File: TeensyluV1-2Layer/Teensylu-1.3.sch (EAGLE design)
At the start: 101 parts, among them J1 M02POLAR, J11 M02POLAR, J12 M02POLAR, J2 MICROSD, J3 USB-MICRO-PTH, J4 M02POLAR, J5 4P-TERM-BLOCK284391-4, J6 39-29-3066, J7 HOTEND-1, J8 2x7, J9 HOTBED, P1 POLOLU-X, P2 POLOLU-Y, P3 POLOLU-Z, P4 POLOLU-E1, Q1 PMV45EN, Q2 PSMN1R2-30YLC, Q3 PSMN1R2-30YLC, Q5 MMUN2211LT3G, U1 LMR16006X, U2 PRTR5V0U4DSOT23-6, U3 AP7313SOT23C, U4 TXB0104TSSOP14, U5 AT90USB1286, X1 16MHZ

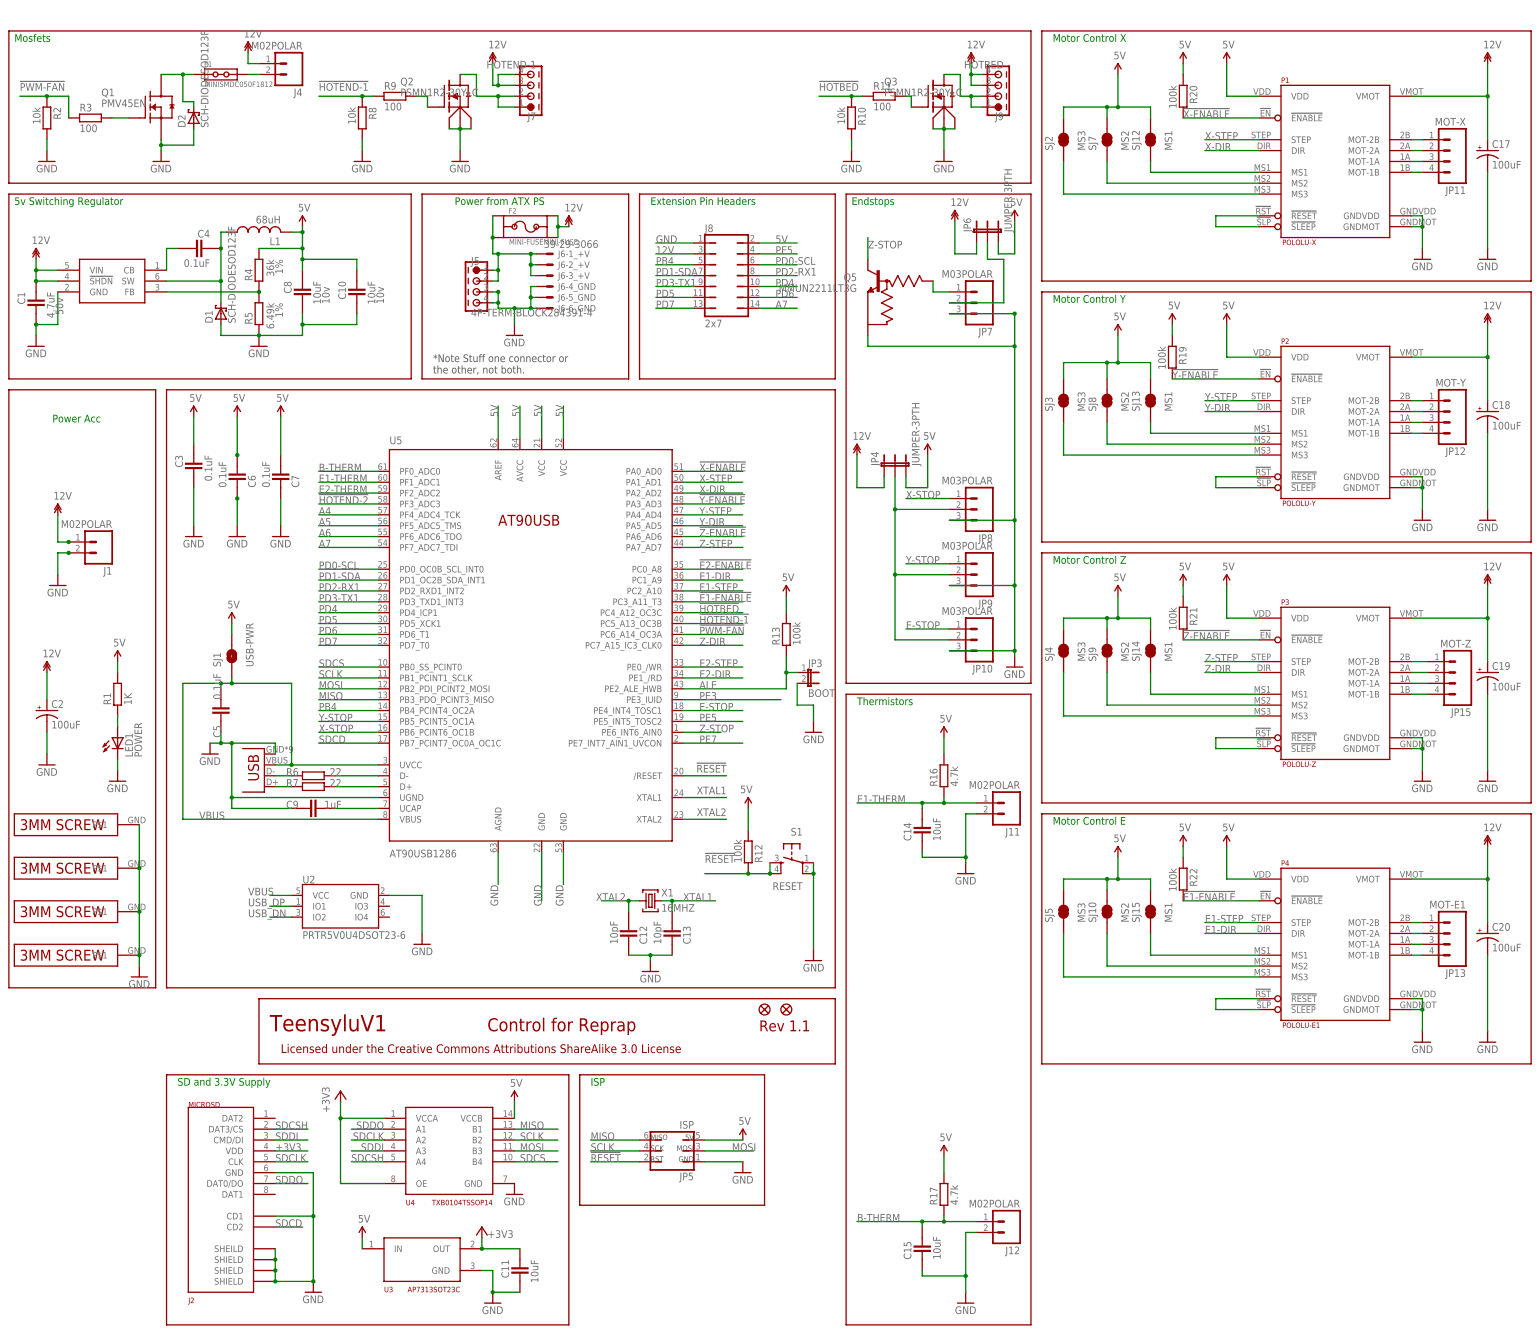
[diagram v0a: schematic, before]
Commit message: Updated USB Diode, Added Jumper Wires, Z Endstop is now 4 pin
The USB Diode has been changed to DRTR5V0U2SR
22ga jumper wires added to increase current capacity
Z Endstop header is now 4 pin. All future versions will use 4 pin
endstop on Z. See schematics and set the appropriate pinout for your
configuration.
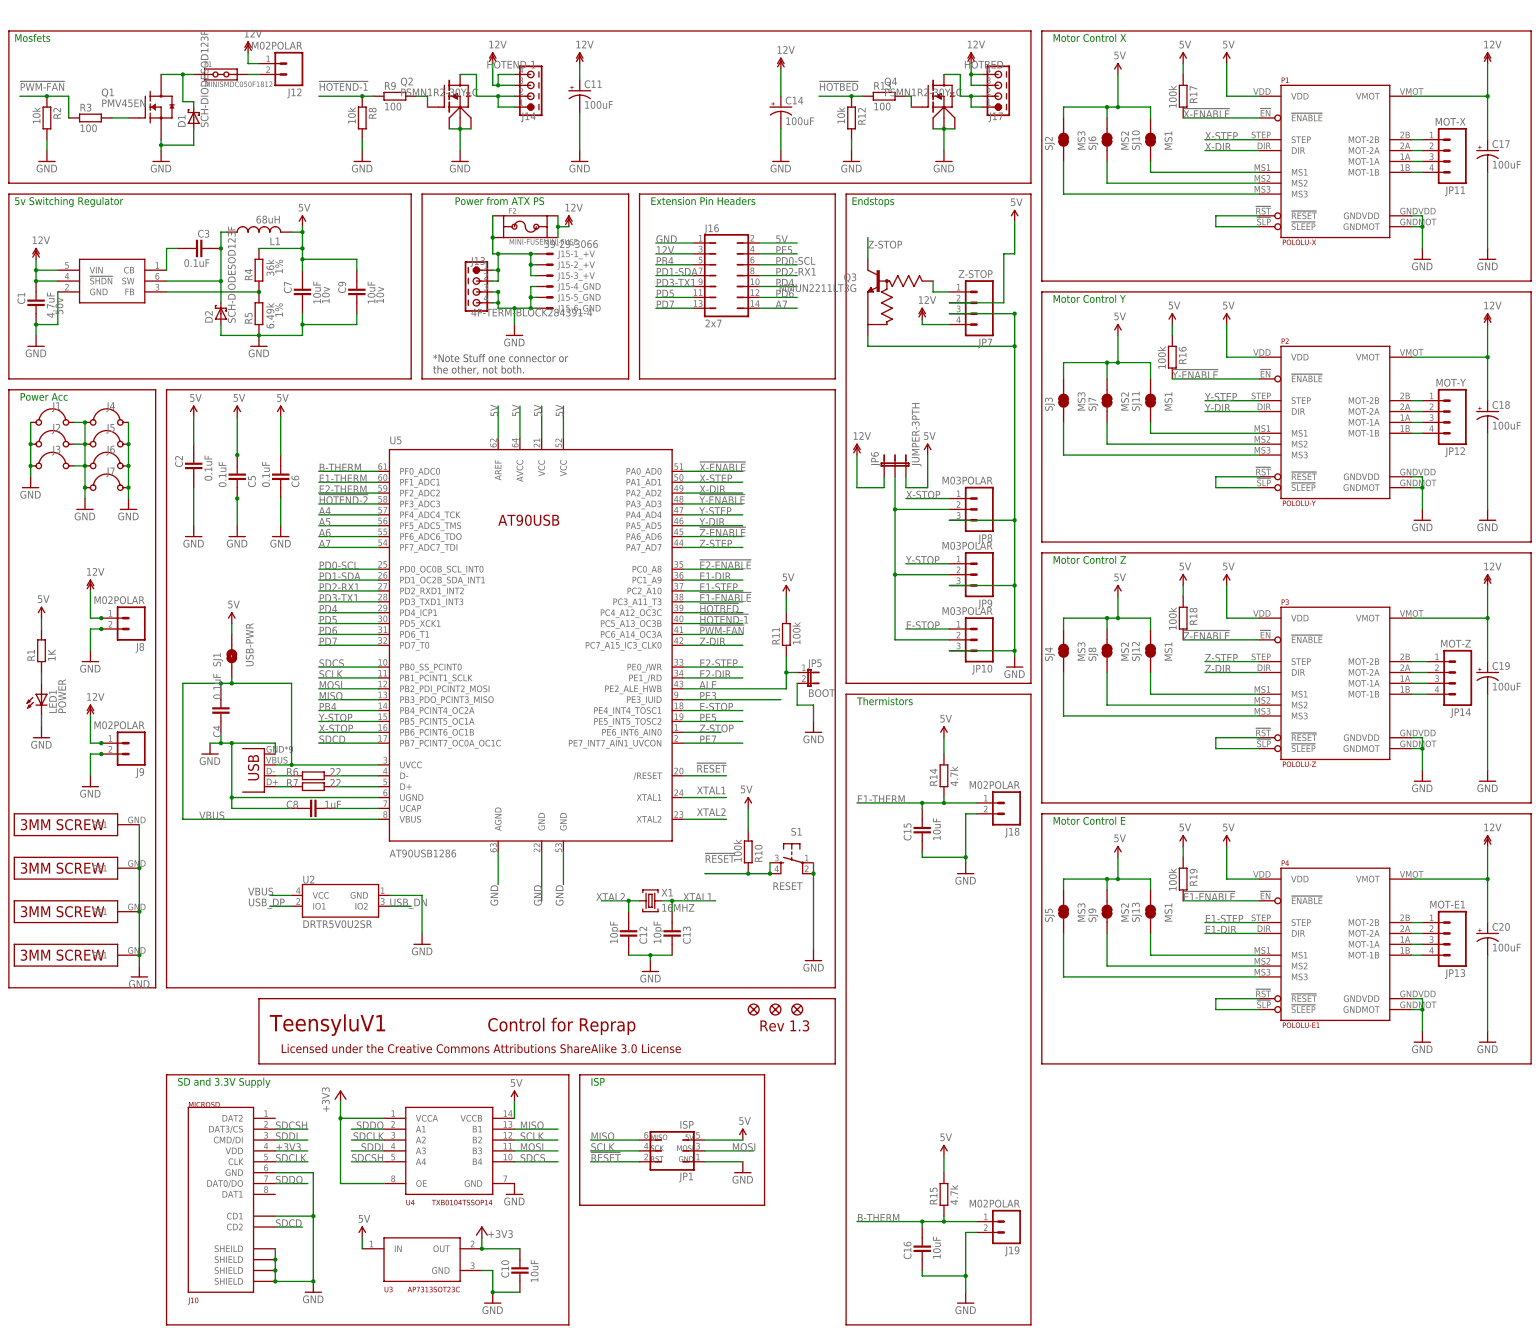
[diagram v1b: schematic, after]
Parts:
- removed Q5: MMUN2211LT3G, teensylu:TRANSISTOR_NPN_BIASSOT23C
- removed R20, R22: 100k, teensylu:RESISTOR_0603
- removed SJ14, SJ15: MS1, teensylu:SOLDERJUMPER-NCSJ-TRACE
- added C16: 10uF, teensylu:CAPACITOR_0603
- added J10: MICROSD, teensylu:MICROSD
- added J13: 4P-TERM-BLOCK284391-4, teensylu:4P-TERM-BLOCK284391-4
- added J14: HOTEND-1, teensylu:4P-TERM-BLOCK284391-4
- added J15: 39-29-3066, teensylu:39-29-3066
- added J16: 2x7, teensylu:JP7Q
- added J17: HOTBED, teensylu:4P-TERM-BLOCK284391-4
- added J18, J19: M02POLAR, teensylu:M02POLAR
- added Q4: PSMN1R2-30YLC, teensylu:PSMN1R2-30YLCPOWERPACK-S08
- added R14, R15: 4.7k, teensylu:RESISTOR_0603
- added SJ11: MS1, teensylu:SOLDERJUMPER-NCSJ-TRACE
- added SJ6: MS2, teensylu:SOLDERJUMPER-NCSJ-TRACE
- C10: device teensylu:CAPACITOR_0805 -> teensylu:CAPACITOR_0603; ESR 0.0030 -> (none); MANUFACTURER_PART_NUMBER GRM21BR71A106KE51L -> GRM188R61C106MA73D; TOLERANCE 10% -> 20%; VDC 10v -> 16V
- C11, C14: value 10uF -> 100uF; device teensylu:CAPACITOR_0603 -> teensylu:CPOL-USD; MANUFACTURER Murata -> Panasonic; MANUFACTURER_PART_NUMBER GRM188R61C106MA73D -> EEE-FTH101XAP; VDC 16V -> 50v
- C2: value 100uF -> 0.1uF; device teensylu:CPOL-USD -> teensylu:CAPACITOR_0603; MANUFACTURER Panasonic -> Murata; MANUFACTURER_PART_NUMBER EEE-FTH101XAP -> GRM188R71C104KA01D; TOLERANCE 20% -> 10%; VDC 50v -> 16V
- C3: MANUFACTURER Murata -> Samsung; MANUFACTURER_PART_NUMBER GRM188R71C104KA01D -> CL10B104KB8NNNC; VDC 16V -> 50V
- C4: MANUFACTURER Samsung -> Murata; MANUFACTURER_PART_NUMBER CL10B104KB8NNNC -> GRM188R71C104KA01D; VDC 50V -> 16V
- C7: value 0.1uF -> 10uF; device teensylu:CAPACITOR_0603 -> teensylu:CAPACITOR_0805; ESR (none) -> 0.0030; MANUFACTURER_PART_NUMBER GRM188R71C104KA01D -> GRM21BR71A106KE51L; VDC 16V -> 10v
- C8: value 10uF -> 1uF; device teensylu:CAPACITOR_0805 -> teensylu:CAPACITOR_0603; ESR 0.0030 -> (none); MANUFACTURER Murata -> Samsung; MANUFACTURER_PART_NUMBER GRM21BR71A106KE51L -> CL10A105MO8NNNC; TOLERANCE 10% -> 20%; VDC 10v -> 16V
- C9: value 1uF -> 10uF; device teensylu:CAPACITOR_0603 -> teensylu:CAPACITOR_0805; ESR (none) -> 0.0030; MANUFACTURER Samsung -> Murata; MANUFACTURER_PART_NUMBER CL10A105MO8NNNC -> GRM21BR71A106KE51L; TOLERANCE 20% -> 10%; VDC 16V -> 10v
- D1: MANUFACTURER_PART_NUMBER PMEG4010CEH,115 -> (none); REVERSE_VOLTAGE 40V -> (none)
- D2: MANUFACTURER_PART_NUMBER (none) -> PMEG4010CEH,115; REVERSE_VOLTAGE (none) -> 40V
- J1, J4: value M02POLAR -> 22ga; device teensylu:M02POLAR -> teensylu:WIRE_JUMPER-0.1; DESCRIPTION CONN HEADER 2POS .100 VERT TIN -> 22ga jumper wire; MANUFACTURER Molex -> N/A; MANUFACTURER_PART_NUMBER 0022272021 -> N/A; NOTES Can use alternative part for Right Angle. MFG: TE Connectiv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 -> (none)
- J11: value M02POLAR -> USB-MICRO-PTH; device teensylu:M02POLAR -> teensylu:USB-MICRO-PTH; DESCRIPTION CONN HEADER 2POS .100 VERT TIN -> (none); MANUFACTURER Molex -> (none); MANUFACTURER_PART_NUMBER 0022272021 -> (none); NOTES Can use alternative part for Right Angle. MFG: TE Connectiv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 -> (none)
- J2: value MICROSD -> 22ga; device teensylu:MICROSD -> teensylu:WIRE_JUMPER-0.1; DESCRIPTION CONN MICRO SD CARD PUSH-PULL R/A -> 22ga jumper wire; MANUFACTURER (none) -> N/A; MANUFACTURER_PART_NUMBER (none) -> N/A
- J3: value USB-MICRO-PTH -> 22ga; device teensylu:USB-MICRO-PTH -> teensylu:WIRE_JUMPER-0.1; DESCRIPTION (none) -> 22ga jumper wire; MANUFACTURER (none) -> N/A; MANUFACTURER_PART_NUMBER (none) -> N/A
- J5: value 4P-TERM-BLOCK284391-4 -> 22ga; device teensylu:4P-TERM-BLOCK284391-4 -> teensylu:WIRE_JUMPER-0.1; DESCRIPTION (none) -> 22ga jumper wire; MANUFACTURER (none) -> N/A; MANUFACTURER_PART_NUMBER (none) -> N/A
- J6: value 39-29-3066 -> 22ga; device teensylu:39-29-3066 -> teensylu:WIRE_JUMPER-0.1; DESCRIPTION (none) -> 22ga jumper wire; MANUFACTURER (none) -> N/A; MANUFACTURER_PART_NUMBER (none) -> N/A
- J7: value HOTEND-1 -> 22ga; device teensylu:4P-TERM-BLOCK284391-4 -> teensylu:WIRE_JUMPER-0.1; DESCRIPTION (none) -> 22ga jumper wire; MANUFACTURER (none) -> N/A; MANUFACTURER_PART_NUMBER (none) -> N/A
- J8: value 2x7 -> M02POLAR; device teensylu:JP7Q -> teensylu:M02POLAR; DESCRIPTION DIL VERTICAL PC TAIL PIN HEADER -> CONN HEADER 2POS .100 VERT TIN; MANUFACTURER Harwin -> Molex; MANUFACTURER_PART_NUMBER M20-9980746 -> 0022272021; NOTES (none) -> Can use alternative part for Right Angle. MFG: TE Connectiv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
- J9: value HOTBED -> M02POLAR; device teensylu:4P-TERM-BLOCK284391-4 -> teensylu:M02POLAR; DESCRIPTION (none) -> CONN HEADER 2POS .100 VERT TIN; MANUFACTURER (none) -> Molex; MANUFACTURER_PART_NUMBER (none) -> 0022272021; NOTES (none) -> Can use alternative part for Right Angle. MFG: TE Connectiv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
- JP1: value FIDUCIAL1X2.5 -> ISP; device SparkFun:FIDUCIAL1X2.5 -> teensylu:PROGHEADER
- JP3: value BOOT -> FIDUCIAL1X2.5; device teensylu:JUMPER-2PTH -> SparkFun:FIDUCIAL1X2.5; DESCRIPTION SIL VERTICAL PC TAIL PIN HEADER -> (none); MANUFACTURER Harwin -> (none); MANUFACTURER_PART_NUMBER M20-9990246 -> (none)
- JP4: value JUMPER-3PTH -> FIDUCIAL1X2.5; device teensylu:JUMPER-3PTH -> SparkFun:FIDUCIAL1X2.5
- JP5: value ISP -> BOOT; device teensylu:PROGHEADER -> teensylu:JUMPER-2PTH; DESCRIPTION (none) -> SIL VERTICAL PC TAIL PIN HEADER; MANUFACTURER (none) -> Harwin; MANUFACTURER_PART_NUMBER (none) -> M20-9990246
- JP7: value M03POLAR -> Z-STOP; device teensylu:M03POLAR -> teensylu:M04POLAR; DESCRIPTION CONN HEADER 3POS .100 VERT TIN -> (none); MANUFACTURER Molex -> (none); MANUFACTURER_PART_NUMBER 0022272031 -> (none); NOTES Can use alternative part for Right Angle. MFG: TE Connectivity PN: 640455-3 -> Can use alternative part for Right Angle. MFG: TE Connectivity PN: 640455-4
- Q3: value PSMN1R2-30YLC -> MMUN2211LT3G; device teensylu:PSMN1R2-30YLCPOWERPACK-S08 -> teensylu:TRANSISTOR_NPN_BIASSOT23C; DESCRIPTION (none) -> TRANS PREBIAS NPN 246MW SOT23-3; MANUFACTURER (none) -> ON Semiconductor; MANUFACTURER_PART_NUMBER (none) -> MMUN2211LT3G
- R10: value 10k -> 100k
- R11: value 100 -> 100k
- R12: value 100k -> 10k
- R13: value 100k -> 100
- R16, R17: value 4.7k -> 100k
- SJ10: value MS2 -> MS1
- U2: value PRTR5V0U4DSOT23-6 -> DRTR5V0U2SR; device teensylu:PRTR5V0U4DSOT23-6 -> teensylu:DRTR5V0U2SR
- renumbered JP15 to JP14, R21 to R18
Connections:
- removed net Z-STOP-SUPPLY: JP6.2, JP7.2
- net !E1-ENABLE: now also R19.2; no longer R22.2
- net !HOTBED: now also R12.1, R13.1; no longer R10.1, R11.1
- net !RESET: now also JP1.2, R10.1; no longer JP5.2, R12.1
- net !X-ENABLE: now also R17.2; no longer R20.2
- net !Y-ENABLE: now also R16.2; no longer R19.2
- net +3V3: now also C10.1, J10.VDD; no longer C11.1, J2.VDD
- net 12V: now also C11.+, C14.+, J12.1, J14.3, J14.4, J16.3, J17.3, J17.4, J8.1, J9.1, JP7.4; no longer C2.+, J1.1, J4.1, J7.3, J7.4, J8.3, J9.3, J9.4, JP4.1
- net 12V_FUSE: now also J13.1, J13.2, J15-1_+V.S, J15-2_+V.S, J15-3_+V.S; no longer J5.1, J5.2, J6-1_+V.S, J6-2_+V.S, J6-3_+V.S
- net 5V: now also C2.1, C5.2, C7.1, C9.1, J16.2, JP1.5, JP7.2, R10.2, R11.2, R14.2, R15.2, R16.1, R17.1, SJ11.2, SJ6.2; no longer C10.1, C3.1, C7.2, C8.1, J8.2, JP4.3, JP5.5, R12.2, R13.2, R16.2, R17.2, R20.1, R22.1, SJ14.2, SJ15.2
- net 5VREG_CB: now also C3.2; no longer C4.2
- net 5VREG_SW: now also C3.1, D2.C; no longer C4.1, D1.C
- net A7: now also J16.14; no longer J8.14
- net ALE: now also JP5.1, R11.1; no longer JP3.1, R13.1
- net B-THERM: now also C16.2, J19.1, R15.1; no longer C15.2, J12.1, R17.1
- net E-MS1: now also SJ13.1; no longer SJ15.1
- net E-MS2: now also SJ9.1; no longer SJ10.1
- net E1-THERM: now also C15.2, J18.1, R14.1; no longer C14.2, J11.1, R16.1
- net ENDSTOP+V: now also JP6.2; no longer JP4.2
- net GND: now also C11.-, C14.-, C16.1, C2.2, C4.1, C7.2, C8.1, C9.2, J1.+, J1.-, J10.CD1, J10.GND, J10.SHEILD@1, J10.SHIELD@2, J10.SHIELD@3, J10.SHIELD@4, J11.GND, J13.3, J13.4, J15-4_GND.S, J15-5_GND.S, J15-6_GND.S, J16.1, J18.2, J19.2, J2.+, J2.-, J3.+, J3.-, J4.+, J4.-, J5.+, J5.-, J6.+, J6.-, J7.+, J7.-, J8.2, J9.2, JP1.1, JP5.2, Q3.E, Q4.S1, Q4.S2, Q4.S3, R12.2; no longer C11.2, C14.1, C2.-, C3.2, C7.1, C8.2, C9.1, J1.2, J11.2, J12.2, J2.CD1, J2.GND, J2.SHEILD@1, J2.SHIELD@2, J2.SHIELD@3, J2.SHIELD@4, J3.GND, J5.3, J5.4, J6-4_GND.S, J6-5_GND.S, J6-6_GND.S, J8.1, JP3.2, JP5.1, Q3.S1, Q3.S2, Q3.S3, Q5.E, R10.2
- net HOTBED-GND: now also J17.1, J17.2, Q4.D; no longer J9.1, J9.2, Q3.D
- net HOTEND-GND: now also J14.1, J14.2; no longer J7.1, J7.2
- net MISO: now also JP1.6; no longer JP5.6
- net MOSI: now also JP1.3; no longer JP5.3
- net N$2: now also Q4.G, R13.2; no longer Q3.G, R11.2
- net N$5: now also J12.2; no longer J4.2
- net N$6: now also D1.C; no longer D2.C
- net PB4: now also J16.5; no longer J8.5
- net PD0-SCL: now also J16.6; no longer J8.6
- net PD1-SDA: now also J16.7; no longer J8.7
- net PD2-RX1: now also J16.8; no longer J8.8
- net PD3-TX1: now also J16.9; no longer J8.9
- net PD4: now also J16.10; no longer J8.10
- net PD5: now also J16.11; no longer J8.11
- net PD6: now also J16.12; no longer J8.12
- net PD7: now also J16.13; no longer J8.13
- net PE5: now also J16.4; no longer J8.4
- net SCLK: now also JP1.4; no longer JP5.4
- net SDCD: now also J10.CD2; no longer J2.CD2
- net SDCLK: now also J10.CLK; no longer J2.CLK
- net SDCSH: now also J10.DAT3/CS; no longer J2.DAT3/CS
- net SDDI: now also J10.CMD/DI; no longer J2.CMD/DI
- net SDDO: now also J10.DAT0/DO; no longer J2.DAT0/DO
- net UCAP: now also C8.2; no longer C9.2
- net USB_DN: now also J11.D-; no longer J3.D-
- net USB_DP: now also J11.D+; no longer J3.D+
- net VBUS: now also C4.2, J11.VBUS; no longer C5.2, J3.VBUS
- net X-MS1: now also SJ10.1; no longer SJ12.1
- net X-MS2: now also SJ6.1; no longer SJ7.1
- net Y-MS1: now also SJ11.1; no longer SJ13.1
- net Y-MS2: now also SJ7.1; no longer SJ8.1
- net Z-MS1: now also SJ12.1; no longer SJ14.1
- net Z-MS2: now also SJ8.1; no longer SJ9.1
- net Z-STOP: now also Q3.C; no longer Q5.C
- net Z-STOP-BIAS: now also Q3.B; no longer Q5.B
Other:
- note added: "Rev 1.3"
- note removed: "Rev 1.1"
- moved on the sheet: C10, C15, C3, C4, C5, C6, C7, C8, C9, D1, D2, J12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
